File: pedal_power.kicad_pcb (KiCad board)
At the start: 2 copper layers, 34 x 99.5 mm, 22 parts, among them J1 L, J2 N, J3 Barrel_Jack, J4 Barrel_Jack, J5 Barrel_Jack, J6 Barrel_Jack, U1 L78S09CV

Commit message: tidy up schematic
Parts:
- C1, C2: value C -> 820uF 35V 1.74A
- C3: value CP -> 330uF 25V
- D3: value 24V -> 22/24/35.5V
- U1: value L78S09CV -> L78M09CV
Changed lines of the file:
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@@
       (effects (font (size 1 1) (thickness 0.15)))
     )
-    (fp_text value CP (at 1.75 5.25) (layer F.Fab)
+    (fp_text value "330uF 25V" (at 1.75 5.25) (layer F.Fab)
       (effects (font (size 1 1) (thickness 0.15)))
     )
@@
       (effects (font (size 1 1) (thickness 0.15)))
     )
-    (fp_text value L78S09CV (at 2.54 2) (layer F.Fab)
+    (fp_text value L78M09CV (at 2.54 2) (layer F.Fab)
       (effects (font (size 1 1) (thickness 0.15)))
     )
@@
       (effects (font (size 1 1) (thickness 0.15)))
     )
-    (fp_text value C (at 2.5 7.5) (layer F.Fab)
+    (fp_text value "820uF 35V 1.74A" (at 2.5 7.5) (layer F.Fab)
       (effects (font (size 1 1) (thickness 0.15)))
     )
@@
       (effects (font (size 1 1) (thickness 0.15)))
     )
-    (fp_text value 24V (at 6.35 5.67) (layer F.Fab)
+    (fp_text value 22/24/35.5V (at 6.35 5.67) (layer F.Fab)
       (effects (font (size 1 1) (thickness 0.15)))
     )
@@
       (effects (font (size 1 1) (thickness 0.15)))
     )
-    (fp_text value C (at 2.5 7.5) (layer F.Fab)
-      (effects (font (size 1 1) (thickness 0.15)))
-    )
+    (fp_text value "820uF 35V 1.74A" (at 2.5 7.5) (layer F.Fab)
+      (effects (font (size 1 1) (thickness 0.15)))
+    )

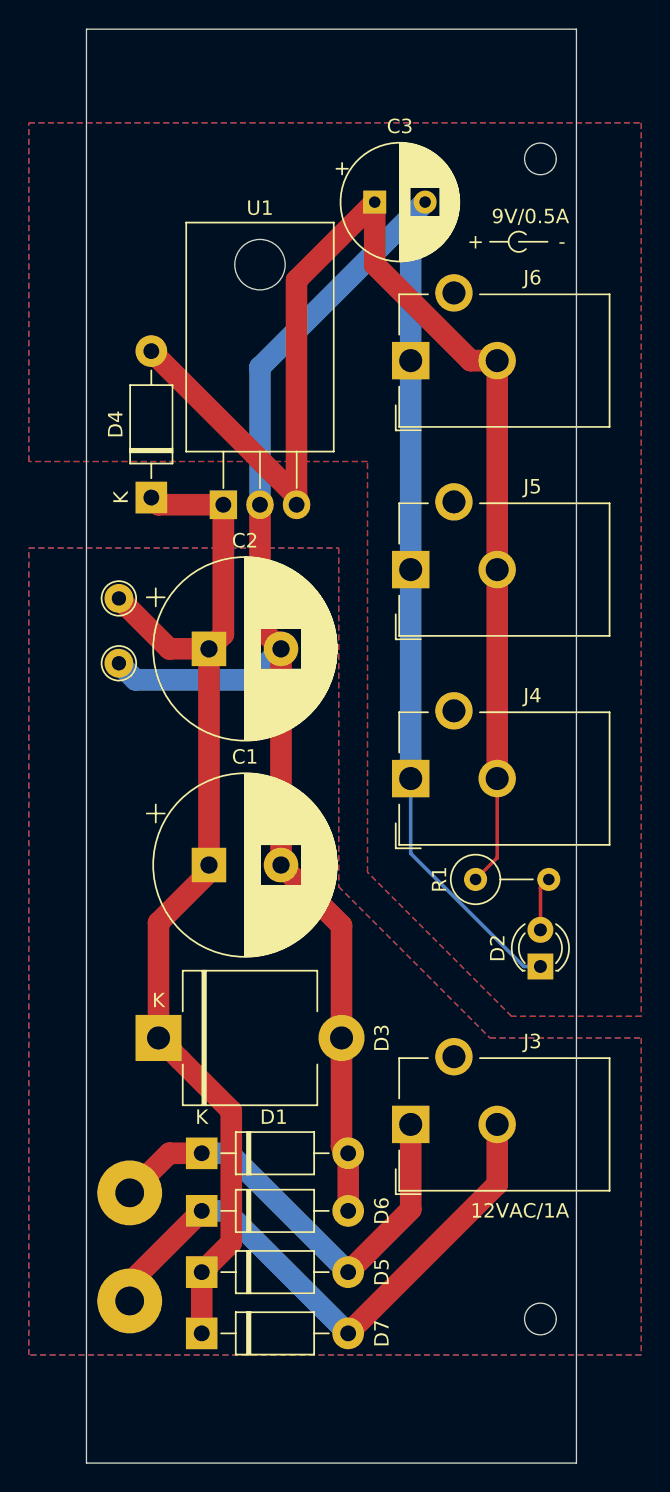
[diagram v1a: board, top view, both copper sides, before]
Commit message: update to kicad 7 and add plot workflow
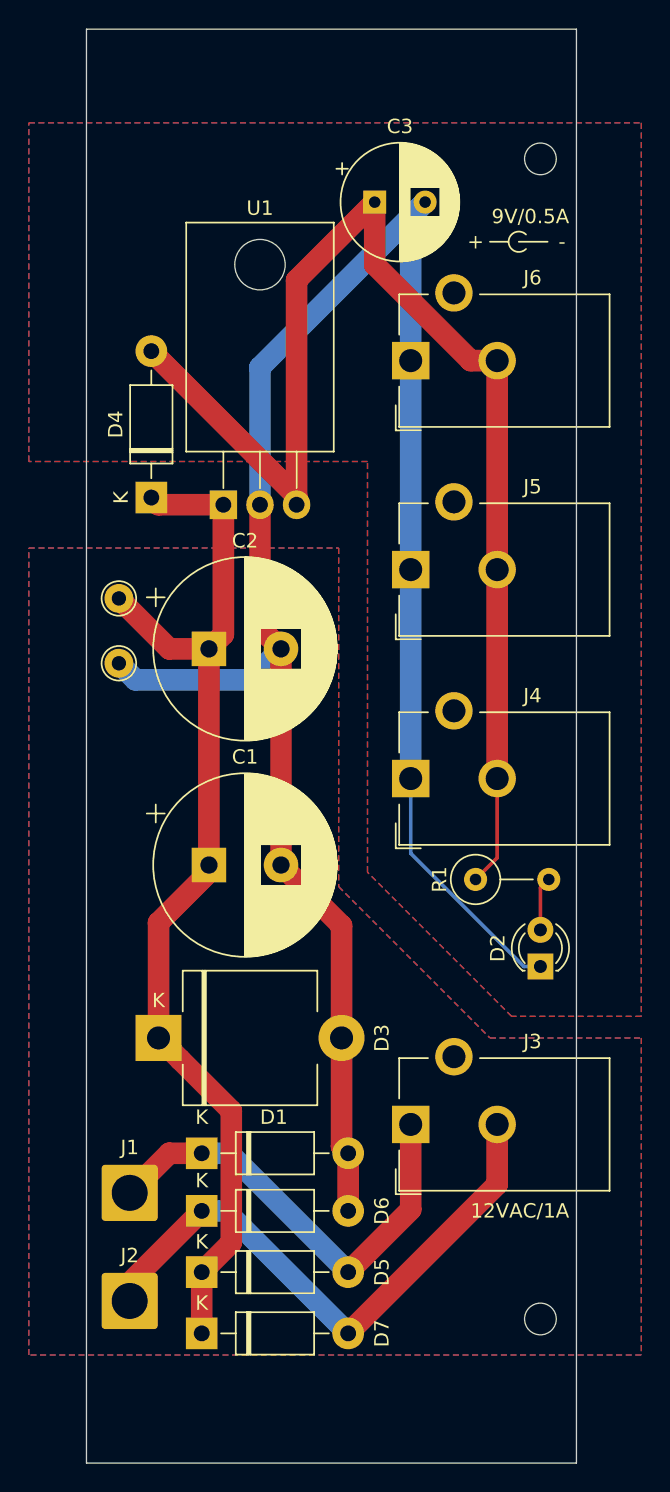
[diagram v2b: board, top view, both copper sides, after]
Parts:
- J1, J2: footprint Connector_Wire:SolderWirePad_1x01_Drill2mm -> Connector_Wire:SolderWire-2sqmm_1x01_D2mm_OD3.9mm
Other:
- net class Default removed
